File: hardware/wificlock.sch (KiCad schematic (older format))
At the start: 41 parts, among them J1 USB_C_Receptacle_USB2.0, Q1 AO3402, Q2 AO3402, Q3 AO3402, Q4 AO3402, SW1 SW_SPST, SW2 SW_SPST, SW3 SW_SPST, U1 CH340C/G, U2 ESP-12F, U3 ME6211C33M5G, U4 HT16K33-20SOP, U5 KW4-56NCLB-P, Y1 12MHz

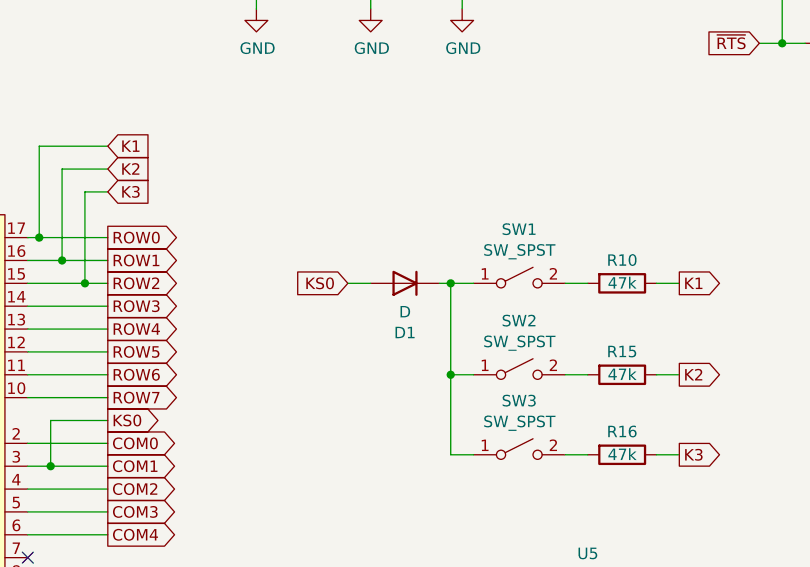
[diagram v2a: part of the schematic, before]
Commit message: use correct diode model
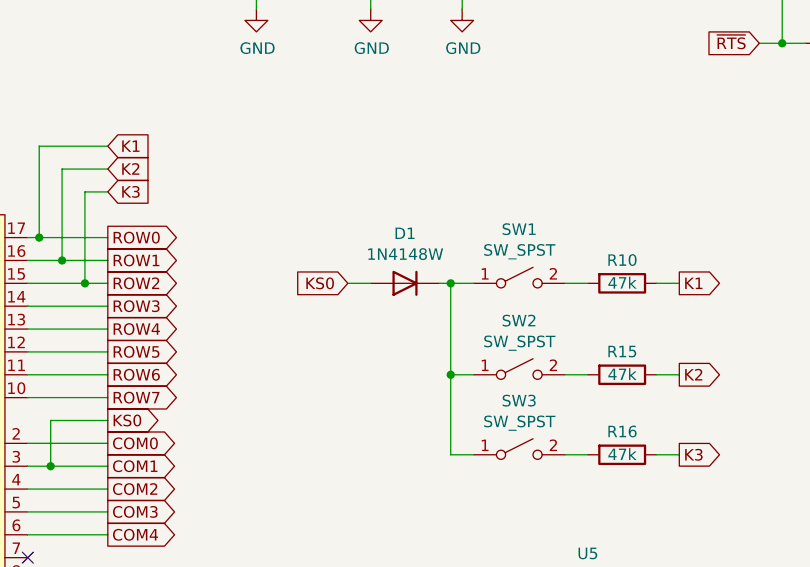
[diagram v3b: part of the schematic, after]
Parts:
- removed D1: D, Diode_SMD:D_SOD-123, symbol Device:D
- added D1: 1N4148W, Diode_SMD:D_SOD-123, symbol Diode:1N4148W
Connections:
- net COM1: now also D1.2 (A)
- net at SW1.1 (A), SW2.1 (A), SW3.1 (A): now also D1.1 (K)
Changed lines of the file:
@@
 KS0
-$Comp
-L Device:D D1
-U 1 1 60484D0D
-P 4350 5000
-F 0 "D1" H 4350 5217 50  0000 C CNN
-F 1 "D" H 4350 5126 50  0000 C CNN
-F 2 "Diode_SMD:D_SOD-123" H 4350 5000 50  0001 C CNN
-F 3 "~" H 4350 5000 50  0001 C CNN
-	1    4350 5000
-	-1   0    0    1
-$EndComp
 $Comp
 L Switch:SW_SPST SW1
@@
 	1    0    0    -1
 $EndComp
+$Comp
+L Diode:1N4148W D1
+U 1 1 6066433F
+P 4350 5000
+F 0 "D1" H 4350 4783 50  0000 C CNN
+F 1 "1N4148W" H 4350 4874 50  0000 C CNN
+F 2 "Diode_SMD:D_SOD-123" H 4350 4825 50  0001 C CNN
+F 3 "https://www.vishay.com/docs/85748/1n4148w.pdf" H 4350 5000 50  0001 C CNN
+	1    4350 5000
+	-1   0    0    1
+$EndComp
 $EndSCHEMATC

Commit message: add 3D models for footprints
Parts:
- SW1, SW2, SW3: footprint wificlock:Switch-Tactile-3x6x3.5 -> wificlock:SW_SPST_SMD_3x6x3.5_Side
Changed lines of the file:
@@
 F 0 "SW1" H 4850 5235 50  0000 C CNN
 F 1 "SW_SPST" H 4850 5144 50  0000 C CNN
-F 2 "wificlock:Switch-Tactile-3x6x3.5" H 4850 5000 50  0001 C CNN
+F 2 "wificlock:SW_SPST_SMD_3x6x3.5_Side" H 4850 5000 50  0001 C CNN
 F 3 "~" H 4850 5000 50  0001 C CNN
 	1    4850 5000
@@
 F 0 "SW2" H 4850 5635 50  0000 C CNN
 F 1 "SW_SPST" H 4850 5544 50  0000 C CNN
-F 2 "wificlock:Switch-Tactile-3x6x3.5" H 4850 5400 50  0001 C CNN
+F 2 "wificlock:SW_SPST_SMD_3x6x3.5_Side" H 4850 5400 50  0001 C CNN
 F 3 "~" H 4850 5400 50  0001 C CNN
 	1    4850 5400
@@
 F 0 "SW3" H 4850 5985 50  0000 C CNN
 F 1 "SW_SPST" H 4850 5894 50  0000 C CNN
-F 2 "wificlock:Switch-Tactile-3x6x3.5" H 4850 5750 50  0001 C CNN
+F 2 "wificlock:SW_SPST_SMD_3x6x3.5_Side" H 4850 5750 50  0001 C CNN
 F 3 "~" H 4850 5750 50  0001 C CNN
 	1    4850 5750
